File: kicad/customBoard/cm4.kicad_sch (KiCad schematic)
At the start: 17 parts

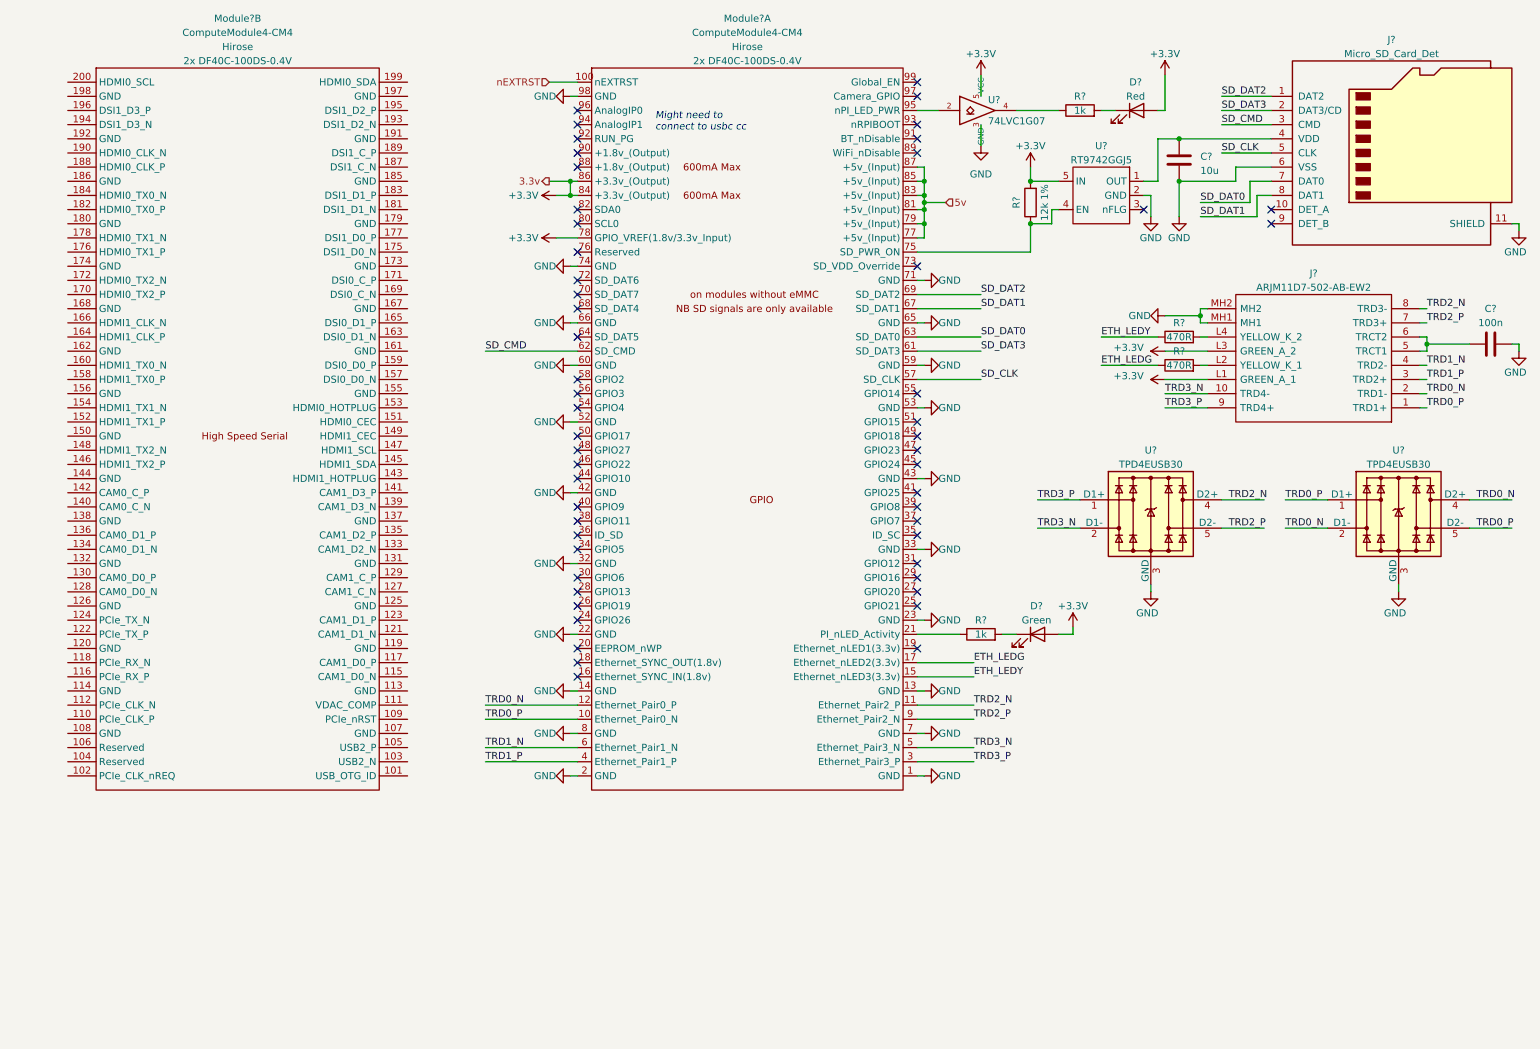
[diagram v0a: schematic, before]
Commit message: Draft CM4 High Speed Serial
One interesting dilemma that has come up is how to handle replacements for the RT9742 part. Since the ones I was originally going to use are out of stock, an exciting hunt occurred to find a replacement that will not break anything. After some meetings and some investigation, I believe some good replacements have been found. For future reference, the documentation has been included in the notes folder
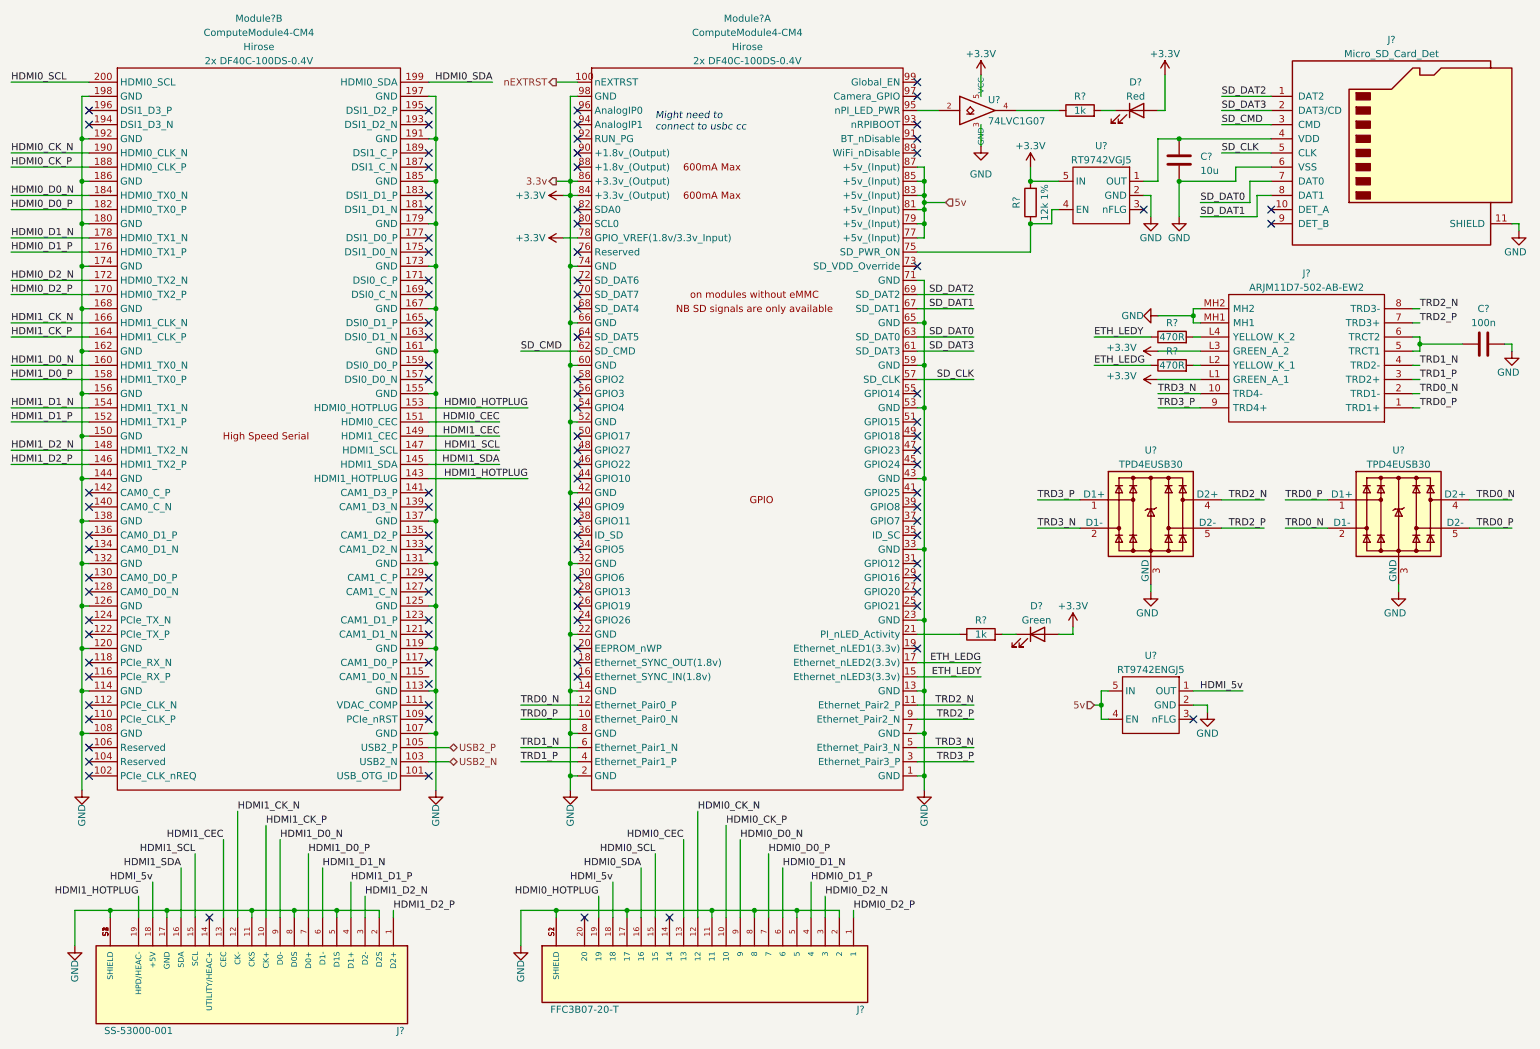
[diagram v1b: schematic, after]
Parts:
- added J?: SS-53000-001, STEWART_SS-53000-001, symbol SS-53000-001:SS-53000-001
- added J?: FFC3B07-20-T, GCT_FFC3B07-20-T, symbol FFC3B07-20-T:FFC3B07-20-T
- added U?: RT9742ENGJ5, Package_TO_SOT_SMD:SOT-23-5, symbol rt9742ggj5:RT9742GGJ5
- U?: value RT9742GGJ5 -> RT9742VGJ5
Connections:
- net GND is gone; now on net +3V3: C?.2, C?.2, J?.11 (SHIELD), J?.6 (VSS), J?.MH1, J?.MH2, Module?.1 (GND), Module?.13 (GND), Module?.14 (GND), Module?.2 (GND), Module?.22 (GND), Module?.23 (GND), Module?.32 (GND), Module?.33 (GND), Module?.42 (GND), Module?.43 (GND), Module?.52 (GND), Module?.53 (GND), Module?.59 (GND), Module?.60 (GND), Module?.65 (GND), Module?.66 (GND), Module?.7 (GND), Module?.71 (GND), Module?.74 (GND), Module?.8 (GND), Module?.98 (GND), U?.2 (GND), U?.3 (GND), U?.3 (GND), U?.3 (GND), U?.8 (GND), U?.8 (GND)
- net +3V3: now also Module?.107 (GND), Module?.108 (GND), Module?.113 (GND), Module?.114 (GND), Module?.119 (GND), Module?.120 (GND), Module?.125 (GND), Module?.126 (GND), Module?.131 (GND), Module?.132 (GND), Module?.137 (GND), Module?.138 (GND), Module?.144 (GND), Module?.150 (GND), Module?.155 (GND), Module?.156 (GND), Module?.161 (GND), Module?.162 (GND), Module?.167 (GND), Module?.168 (GND), Module?.173 (GND), Module?.174 (GND), Module?.179 (GND), Module?.180 (GND), Module?.185 (GND), Module?.186 (GND), Module?.191 (GND), Module?.192 (GND), Module?.197 (GND), Module?.198 (GND), J?.11, J?.11 (CKS), J?.17, J?.17 (GND), J?.2, J?.2 (D2S), J?.5, J?.5 (D1S), J?.8, J?.8 (D0S), J?.S1 (SHIELD), J?.S1 (SHIELD), J?.S2 (SHIELD), J?.S2 (SHIELD), J?.S3 (SHIELD), J?.S4 (SHIELD), U?.2 (GND)
- net 5v: now also U?.4 (EN), U?.5 (IN)
- net USB2_N: now reaches Module?.103 (USB2_N)
- net USB2_P: now reaches Module?.105 (USB2_P)
- net HDMI1_HOTPLUG: now reaches Module?.143 (HDMI1_HOTPLUG)
- net HDMI1_HOTPLUG: now also J?.19 (HPD/HEAC-)
- net HDMI1_SDA: now reaches Module?.145 (HDMI1_SDA)
- net HDMI1_SDA: now also J?.16 (SDA)
- net HDMI1_D2_P: now reaches Module?.146 (HDMI1_TX2_P)
- net HDMI1_D2_P: now also J?.1 (D2+)
- net HDMI1_SCL: now reaches Module?.147 (HDMI1_SCL)
- net HDMI1_SCL: now also J?.15 (SCL)
- net HDMI1_D2_N: now reaches Module?.148 (HDMI1_TX2_N)
- net HDMI1_D2_N: now also J?.3 (D2-)
- net HDMI1_CEC: now reaches Module?.149 (HDMI1_CEC)
- net HDMI1_CEC: now also J?.13 (CEC)
- net HDMI0_CEC: now reaches Module?.151 (HDMI0_CEC)
- net HDMI0_CEC: now also J?.13
- net HDMI1_D1_P: now reaches Module?.152 (HDMI1_TX1_P)
- net HDMI1_D1_P: now also J?.4 (D1+)
- net HDMI0_HOTPLUG: now reaches Module?.153 (HDMI0_HOTPLUG)
- net HDMI0_HOTPLUG: now also J?.19
- net HDMI1_D1_N: now reaches Module?.154 (HDMI1_TX1_N)
- net HDMI1_D1_N: now also J?.6 (D1-)
- net HDMI1_D0_P: now reaches Module?.158 (HDMI1_TX0_P)
- net HDMI1_D0_P: now also J?.7 (D0+)
- net HDMI1_D0_N: now reaches Module?.160 (HDMI1_TX0_N)
- net HDMI1_D0_N: now also J?.9 (D0-)
- net HDMI1_CK_P: now reaches Module?.164 (HDMI1_CLK_P)
- net HDMI1_CK_P: now also J?.10 (CK+)
- net HDMI1_CK_N: now reaches Module?.166 (HDMI1_CLK_N)
- net HDMI1_CK_N: now also J?.12 (CK-)
- net HDMI0_D2_P: now reaches Module?.170 (HDMI0_TX2_P)
- net HDMI0_D2_P: now also J?.1
- net HDMI0_D2_N: now reaches Module?.172 (HDMI0_TX2_N)
- net HDMI0_D2_N: now also J?.3
- net HDMI0_D1_P: now reaches Module?.176 (HDMI0_TX1_P)
- net HDMI0_D1_P: now also J?.4
- net HDMI0_D1_N: now reaches Module?.178 (HDMI0_TX1_N)
- net HDMI0_D1_N: now also J?.6
- net HDMI0_D0_P: now reaches Module?.182 (HDMI0_TX0_P)
- net HDMI0_D0_P: now also J?.7
- net HDMI0_D0_N: now reaches Module?.184 (HDMI0_TX0_N)
- net HDMI0_D0_N: now also J?.9
- net HDMI0_CK_P: now reaches Module?.188 (HDMI0_CLK_P)
- net HDMI0_CK_P: now also J?.10
- net HDMI0_CK_N: now reaches Module?.190 (HDMI0_CLK_N)
- net HDMI0_CK_N: now also J?.12
- net HDMI0_SDA: now reaches Module?.199 (HDMI0_SDA)
- net HDMI0_SDA: now also J?.16
- net HDMI0_SCL: now reaches Module?.200 (HDMI0_SCL)
- net HDMI0_SCL: now also J?.15
- new net HDMI_5v: J?.18, J?.18 (+5V), U?.1 (OUT)
- no-connect marks 53 -> 101
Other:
- moved on the sheet: C?, J?, Module?B, R?

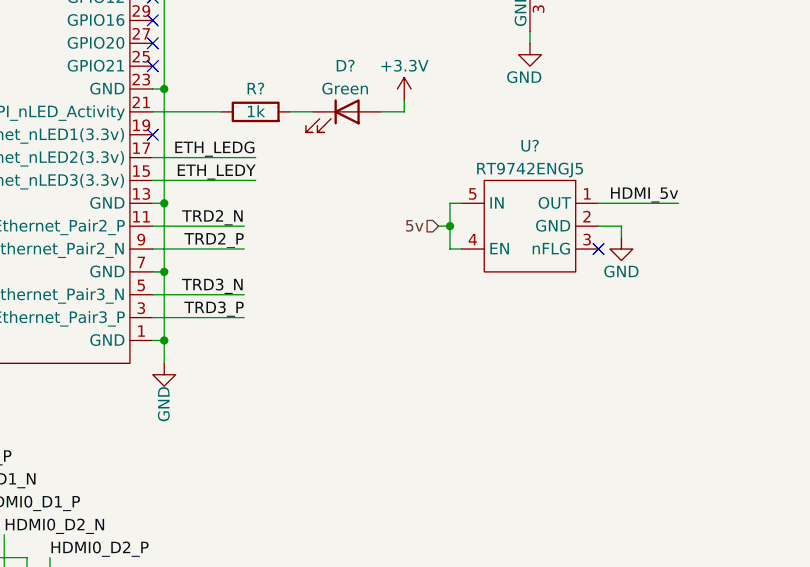
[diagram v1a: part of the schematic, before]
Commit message: First draft of USB
This should complete the first draft of the schematic!
Now time to design the PCB itself
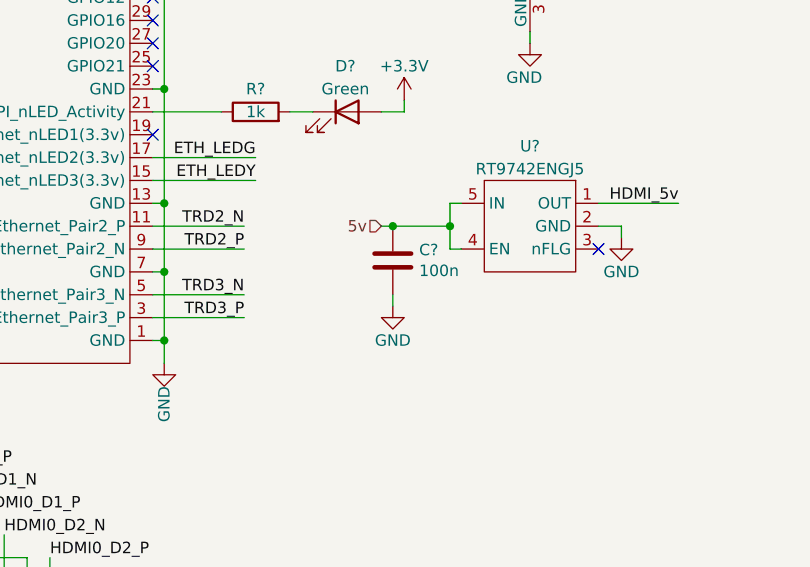
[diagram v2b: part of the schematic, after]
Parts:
- added C?: 100n, Capacitor_SMD:C_0402_1005Metric, symbol Device:C
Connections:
- net +3V3: now also C?.2
- net 5v: now also C?.1
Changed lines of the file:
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@@
   (junction (at 195.58 43.18) (diameter 0.9144) (color 0 0 0 0))
   (junction (at 195.58 50.8) (diameter 0.9144) (color 0 0 0 0))
+  (junction (at 201.93 137.16) (diameter 0.9144) (color 0 0 0 0))
   (junction (at 208.28 137.16) (diameter 0.9144) (color 0 0 0 0))
   (junction (at 222.25 35.56) (diameter 0.9144) (color 0 0 0 0))
@@
     (stroke (width 0) (type solid) (color 0 0 0 0))
   )
+  (wire (pts (xy 200.66 137.16) (xy 201.93 137.16))
+    (stroke (width 0) (type solid) (color 0 0 0 0))
+  )
+  (wire (pts (xy 201.93 137.16) (xy 208.28 137.16))
+    (stroke (width 0) (type solid) (color 0 0 0 0))
+  )
+  (wire (pts (xy 201.93 144.78) (xy 201.93 146.05))
+    (stroke (width 0) (type solid) (color 0 0 0 0))
+  )
   (wire (pts (xy 203.2 124.46) (xy 203.2 123.19))
     (stroke (width 0) (type solid) (color 0 0 0 0))
@@
   )
   (wire (pts (xy 207.01 76.2) (xy 217.17 76.2))
-    (stroke (width 0) (type solid) (color 0 0 0 0))
-  )
-  (wire (pts (xy 207.01 137.16) (xy 208.28 137.16))
     (stroke (width 0) (type solid) (color 0 0 0 0))
   )
@@
     (effects (font (size 1.27 1.27)) (justify left))
   )
-  (hierarchical_label "5v" (shape input) (at 207.01 137.16 180)
+  (hierarchical_label "5v" (shape input) (at 200.66 137.16 180)
     (effects (font (size 1.27 1.27)) (justify right))
   )
@@
     )
     (property "Datasheet" "" (id 3) (at 186.69 36.83 0)
+      (effects (font (size 1.27 1.27)) hide)
+    )
+    (pin "1")
+  )
+  (symbol (lib_id "power:GND") (at 201.93 146.05 0) (unit 1)
+    (in_bom yes) (on_board yes)
+    (property "Reference" "#PWR?" (id 0) (at 201.93 152.4 0)
+      (effects (font (size 1.27 1.27)) hide)
+    )
+    (property "Value" "GND" (id 1) (at 201.93 149.86 0))
+    (property "Footprint" "" (id 2) (at 201.93 146.05 0)
+      (effects (font (size 1.27 1.27)) hide)
+    )
+    (property "Datasheet" "" (id 3) (at 201.93 146.05 0)
       (effects (font (size 1.27 1.27)) hide)
     )
@@
       (effects (font (size 1.27 1.27)) hide)
     )
+    (pin "1")
+    (pin "2")
+  )
+  (symbol (lib_id "Device:C") (at 201.93 140.97 0) (unit 1)
+    (in_bom yes) (on_board yes)
+    (property "Reference" "C?" (id 0) (at 204.851 139.8016 0)
+      (effects (font (size 1.27 1.27)) (justify left))
+    )
+    (property "Value" "100n" (id 1) (at 204.851 142.113 0)
+      (effects (font (size 1.27 1.27)) (justify left))
+    )
+    (property "Footprint" "Capacitor_SMD:C_0402_1005Metric" (id 2) (at 202.8952 144.78 0)
+      (effects (font (size 1.27 1.27)) hide)
+    )
+    (property "Datasheet" "https://search.murata.co.jp/Ceramy/image/img/A01X/G101/ENG/GRM155R71C104KA88-01.pdf" (id 3) (at 201.93 140.97 0)
+      (effects (font (size 1.27 1.27)) hide)
+    )
+    (property "Field4" "Farnell" (id 4) (at 201.93 140.97 0)
+      (effects (font (size 1.27 1.27)) hide)
+    )
+    (property "Field5" "2611911" (id 5) (at 201.93 140.97 0)
+      (effects (font (size 1.27 1.27)) hide)
+    )
+    (property "Field6" "RM EMK105 B7104KV-F" (id 6) (at 201.93 140.97 0)
+      (effects (font (size 1.27 1.27)) hide)
+    )
+    (property "Field7" "TAIYO YUDEN EUROPE GMBH" (id 7) (at 201.93 140.97 0)
+      (effects (font (size 1.27 1.27)) hide)
+    )
+    (property "Part Description" "	0.1uF 10% 16V Ceramic Capacitor X7R 0402 (1005 Metric)" (id 8) (at 201.93 140.97 0)
+      (effects (font (size 1.27 1.27)) hide)
+    )
+    (property "Field8" "110091611" (id 9) (at 201.93 140.97 0)
+      (effects (font (size 1.27 1.27)) hide)
+    )

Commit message: Generate Netlist
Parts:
- C7: renamed from C?; footprint Capacitor_SMD:C_0402_1005Metric -> Capacitor_SMD:C_1206_3216Metric_Pad1.33x1.80mm_HandSolder
- C8, C9: renamed from C?; footprint (none) -> Capacitor_SMD:C_1206_3216Metric_Pad1.33x1.80mm_HandSolder
- D5, D6: renamed from D?; footprint (none) -> digikey-footprints:LED_5mm_Radial
- J2: renamed from J?; footprint STEWART_SS-53000-001 -> SS-53000-001:STEWART_SS-53000-001
- J3: renamed from J?; footprint GCT_FFC3B07-20-T -> FFC3B07-20-T:GCT_FFC3B07-20-T
- J4: renamed from J?; footprint (none) -> CM4IO:SDCARD_MOLEX_503398-1892
- J5: renamed from J?; footprint ARJM11D7502ABEW2 -> ARJM11D7-502-AB-EW2:ARJM11D7502ABEW2
- R15, R16, R17, R18, R19: renamed from R?; footprint (none) -> Resistor_SMD:R_1206_3216Metric_Pad1.30x1.75mm_HandSolder
- gave numbers to parts that had none: 6
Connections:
- net +3V3: no longer C7.2, C8.2, C9.2, J2.11 (CKS), J2.17 (GND), J2.2 (D2S), J2.5 (D1S), J2.8 (D0S), J2.S1 (SHIELD), J2.S2 (SHIELD), J2.S3 (SHIELD), J2.S4 (SHIELD), J3.11, J3.17, J3.2, J3.5, J3.8, J3.S1 (SHIELD), J3.S2 (SHIELD), J4.11 (SHIELD), J4.6 (VSS), J5.MH1, J5.MH2, Module1.1 (GND), Module1.107 (GND), Module1.108 (GND), Module1.113 (GND), Module1.114 (GND), Module1.119 (GND), Module1.120 (GND), Module1.125 (GND), Module1.126 (GND), Module1.13 (GND), Module1.131 (GND), Module1.132 (GND), Module1.137 (GND), Module1.138 (GND), Module1.14 (GND), Module1.144 (GND), Module1.150 (GND), Module1.155 (GND), Module1.156 (GND), Module1.161 (GND), Module1.162 (GND), Module1.167 (GND), Module1.168 (GND), Module1.173 (GND), Module1.174 (GND), Module1.179 (GND), Module1.180 (GND), Module1.185 (GND), Module1.186 (GND), Module1.191 (GND), Module1.192 (GND), Module1.197 (GND), Module1.198 (GND), Module1.2 (GND), Module1.22 (GND), Module1.23 (GND), Module1.32 (GND), Module1.33 (GND), Module1.42 (GND), Module1.43 (GND), Module1.52 (GND), Module1.53 (GND), Module1.59 (GND), Module1.60 (GND), Module1.65 (GND), Module1.66 (GND), Module1.7 (GND), Module1.71 (GND), Module1.74 (GND), Module1.8 (GND), Module1.86 (+3.3v_(Output)), Module1.98 (GND), U3.3 (GND), U4.2 (GND), U5.2 (GND), U6.3 (GND), U6.8 (GND), U7.3 (GND), U7.8 (GND)
- new net 3.3v: Module1.86 (+3.3v_(Output))
- new net GND: C7.2, C8.2, C9.2, J2.11 (CKS), J2.17 (GND), J2.2 (D2S), J2.5 (D1S), J2.8 (D0S), J2.S1 (SHIELD), J2.S2 (SHIELD), J2.S3 (SHIELD), J2.S4 (SHIELD), J3.11, J3.17, J3.2, J3.5, J3.8, J3.S1 (SHIELD), J3.S2 (SHIELD), J4.11 (SHIELD), J4.6 (VSS), J5.MH1, J5.MH2, Module1.1 (GND), Module1.107 (GND), Module1.108 (GND), Module1.113 (GND), Module1.114 (GND), Module1.119 (GND), Module1.120 (GND), Module1.125 (GND), Module1.126 (GND), Module1.13 (GND), Module1.131 (GND), Module1.132 (GND), Module1.137 (GND), Module1.138 (GND), Module1.14 (GND), Module1.144 (GND), Module1.150 (GND), Module1.155 (GND), Module1.156 (GND), Module1.161 (GND), Module1.162 (GND), Module1.167 (GND), Module1.168 (GND), Module1.173 (GND), Module1.174 (GND), Module1.179 (GND), Module1.180 (GND), Module1.185 (GND), Module1.186 (GND), Module1.191 (GND), Module1.192 (GND), Module1.197 (GND), Module1.198 (GND), Module1.2 (GND), Module1.22 (GND), Module1.23 (GND), Module1.32 (GND), Module1.33 (GND), Module1.42 (GND), Module1.43 (GND), Module1.52 (GND), Module1.53 (GND), Module1.59 (GND), Module1.60 (GND), Module1.65 (GND), Module1.66 (GND), Module1.7 (GND), Module1.71 (GND), Module1.74 (GND), Module1.8 (GND), Module1.98 (GND), U3.3 (GND), U4.2 (GND), U5.2 (GND), U6.3 (GND), U6.8 (GND), U7.3 (GND), U7.8 (GND)
- no-connect marks 101 -> 102

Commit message: Rework Power PCB and draft SD
Moving things around so they would make sense on the final board. Flipped around some of the power circuit so the battery can be plugged in on the left side to make room for all the ports on the right.
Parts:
- renumbered R15 to R17, R16 to R18, R17 to R19, R18 to R20, R19 to R21
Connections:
- net HDMI0_CEC: now also J2.13 (CEC); no longer J3.13
- net HDMI0_CK_N: now also J2.12 (CK-); no longer J3.12
- net HDMI0_CK_P: now also J2.10 (CK+); no longer J3.10
- net HDMI0_D0_N: now also J2.9 (D0-); no longer J3.9
- net HDMI0_D0_P: now also J2.7 (D0+); no longer J3.7
- net HDMI0_D1_N: now also J2.6 (D1-); no longer J3.6
- net HDMI0_D1_P: now also J2.4 (D1+); no longer J3.4
- net HDMI0_D2_N: now also J2.3 (D2-); no longer J3.3
- net HDMI0_D2_P: now also J2.1 (D2+); no longer J3.1
- net HDMI0_HOTPLUG: now also J2.19 (HPD/HEAC-); no longer J3.19
- net HDMI0_SCL: now also J2.15 (SCL); no longer J3.15
- net HDMI0_SDA: now also J2.16 (SDA); no longer J3.16
- net HDMI1_CEC: now also J3.13; no longer J2.13 (CEC)
- net HDMI1_CK_N: now also J3.12; no longer J2.12 (CK-)
- net HDMI1_CK_P: now also J3.10; no longer J2.10 (CK+)
- net HDMI1_D0_N: now also J3.9; no longer J2.9 (D0-)
- net HDMI1_D0_P: now also J3.7; no longer J2.7 (D0+)
- net HDMI1_D1_N: now also J3.6; no longer J2.6 (D1-)
- net HDMI1_D1_P: now also J3.4; no longer J2.4 (D1+)
- net HDMI1_D2_N: now also J3.3; no longer J2.3 (D2-)
- net HDMI1_D2_P: now also J3.1; no longer J2.1 (D2+)
- net HDMI1_HOTPLUG: now also J3.19; no longer J2.19 (HPD/HEAC-)
- net HDMI1_SCL: now also J3.15; no longer J2.15 (SCL)
- net HDMI1_SDA: now also J3.16; no longer J2.16 (SDA)
